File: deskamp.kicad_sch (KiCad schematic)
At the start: 33 parts, among them J1 Input 01, J2 Input 02, J3 Preamp Out, J4 Selector Switch, J5 LFE, J6 Mute, J7 Sleep, J8 Motor, J9 Power, K1 TQ2-12V, K2 TQ2-12V, K3 TQ2-12V, K4 TQ2-12V, Q1 PN2222A, Q2 PN2222A, Q3 PN2222A, Q4 PN2222A, U1 esp32-wemos-d1-mini, U2 L9110, U3 TSR_1-2433

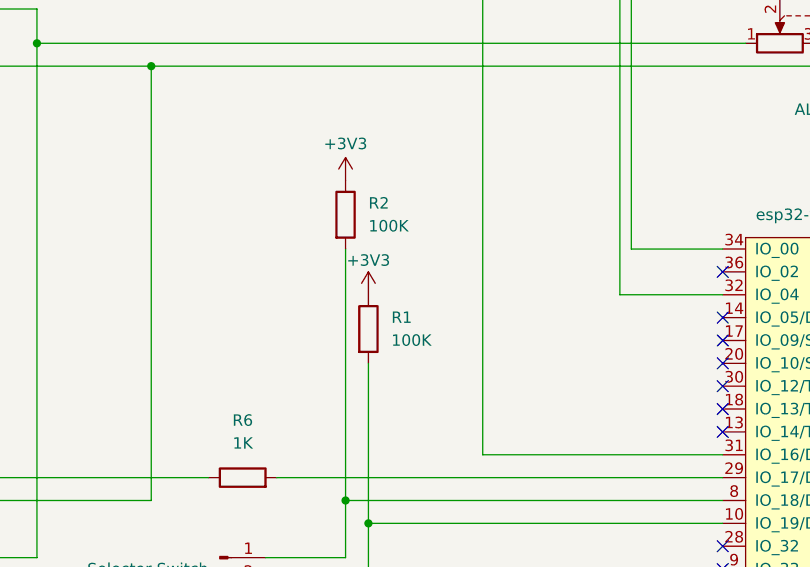
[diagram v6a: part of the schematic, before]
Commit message: Switch to 10K pulldown
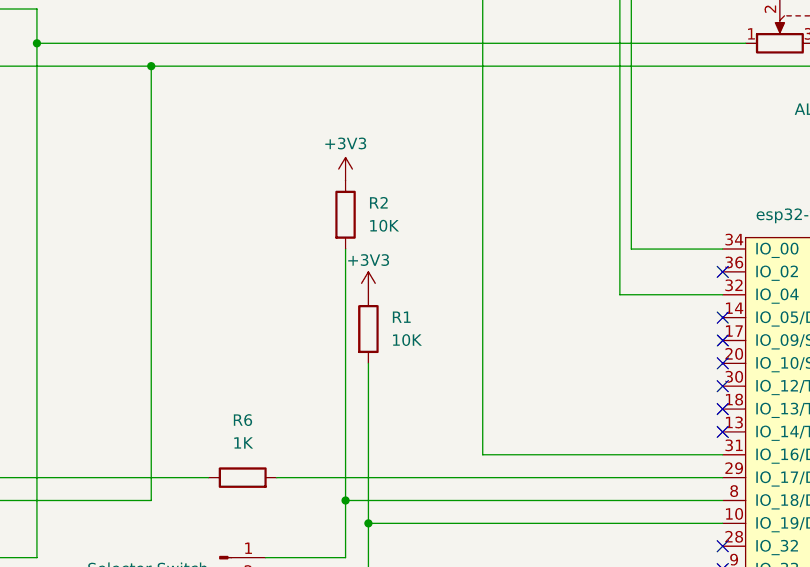
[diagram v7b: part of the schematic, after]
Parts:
- R1, R2: value 100K -> 10K
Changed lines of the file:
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@@
 			)
 		)
-		(property "Value" "100K"
+		(property "Value" "10K"
 			(at 156.21 102.8699 0)
 			(effects
@@
 			)
 		)
-		(property "Value" "100K"
+		(property "Value" "10K"
 			(at 153.67 90.1699 0)
 			(effects

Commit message: Layout stuff.
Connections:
- net GNDA: now also J3.3 (Pin_3), J3.4 (Pin_4); no longer J3.1 (Pin_1), J3.2 (Pin_2)
- net at R3.2, RV1.5: now also J3.1 (Pin_1); no longer J3.3 (Pin_3)
- net at R4.2, RV1.2: now also J3.2 (Pin_2); no longer J3.4 (Pin_4)
